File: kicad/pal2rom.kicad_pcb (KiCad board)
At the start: 2 copper layers, 85 x 100 mm, 11 parts, among them J1 PAL2_Expansion, J4 RIOT+, U1 28C256, U2 74LS145

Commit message: Improve addressing
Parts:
- added C2: .1uF, Capacitor_THT:C_Disc_D5.0mm_W2.5mm_P2.50mm, F.Cu at (138.9, 84.6)
- added JP5: A13_INV, Connector_PinHeader_2.54mm:PinHeader_1x03_P2.54mm_Vertical, F.Cu at (123.7, 115.1)
- added JP6: A12_INV, Connector_PinHeader_2.54mm:PinHeader_1x03_P2.54mm_Vertical, F.Cu at (111.0, 115.1)
- added JP7: A11_INV, Connector_PinHeader_2.54mm:PinHeader_1x03_P2.54mm_Vertical, F.Cu at (98.3, 115.1)
- added R1: 1K2, Resistor_THT:R_Axial_DIN0207_L6.3mm_D2.5mm_P7.62mm_Horizontal, F.Cu at (111.0, 49.0)
- added U3: 74LS04, Package_DIP:DIP-14_W7.62mm, F.Cu at (133.9, 89.7)
- U2: footprint Package_DIP:DIP-16_W7.62mm_Socket -> Package_DIP:DIP-16_W7.62mm
- moved C1 13.2 mm to (126.2, 84.6), turned to 180 degrees
- moved JP1 8.03 mm to (95.8, 99.8)
- moved JP4 8.03 mm to (111.0, 99.8)
- moved JP2 7.62 mm to (108.5, 84.6)
- moved JP3 7.62 mm to (98.3, 84.6)
- moved U2 5.08 mm to (121.2, 89.7)
- renumbered C2 to C3
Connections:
- JP1 pad 1: /~{OE} -> /~{CS}
- JP1 pad 3: /~{OE} -> /~{CS}
- JP1 pad 5: /~{OE} -> /~{CS}
- JP2 pad 4: /AB13 -> Net-(JP2-Pin_4)
- JP4 pad 1: /~{OE} -> /~{CS}
- JP4 pad 2: /~{CS} -> /~{OE}
- U1 pad 2: /AB12 -> /A12
- U1 pad 23: /AB11 -> /A11
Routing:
- net Net-(JP7-Pin_3): track 0.00 -> 102.5 mm
- net /A11: track 0.00 -> 85.3 mm
- net /A13: track 126.2 -> 41.3 mm
- net Net-(JP2-Pin_4): track 0.00 -> 69.7 mm
- net /A12: track 0.00 -> 65.9 mm
- net Net-(JP6-Pin_3): track 0.00 -> 60.6 mm
- net VCC: track 109.6 -> 145.7 mm
- net Net-(JP5-Pin_3): track 0.00 -> 34.0 mm
- net /~{OE}: track 112.1 -> 81.6 mm
- net /AB14: track 34.8 -> 63.8 mm
- net /AB11: track 101.9 -> 130.0 mm
- net /AB15: track 31.8 -> 59.6 mm
- net /AB13: track 57.1 -> 76.8 mm
- net /~{CS}: track 101.1 -> 111.4 mm
- net /8K7_ROM: track 45.2 -> 53.7 mm
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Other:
- board text added: "A11"
- board text added: "A12"
- board text added: "A13"
- board text added: "INVERT ADDRESS"
- board text added: "PAL-2 ROM Board Plastic Objects Limited"
- board text added: "ROM BANK"
- board text added: "Rev 0.1 - 10/2026"
- board text added: "~{A11}"
- board text added: "~{A12}"
- board text added: "~{A13}"
- board text removed: "PAL-2 ROM Whatsit Plastic Objects Limited"
- board text removed: "ROM CONFIG"
- board text removed: "Rev 0 - 10/2026"

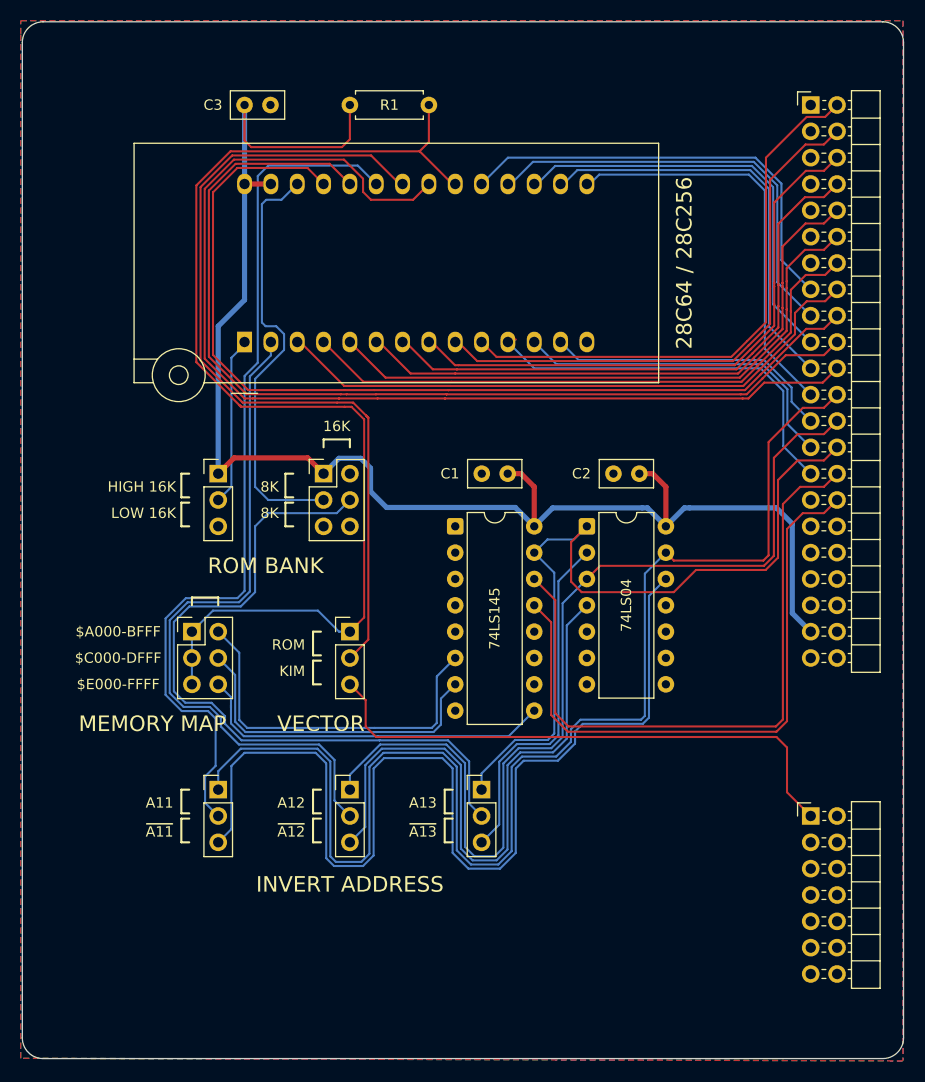
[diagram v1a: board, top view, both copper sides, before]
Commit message: Minor routing improvements
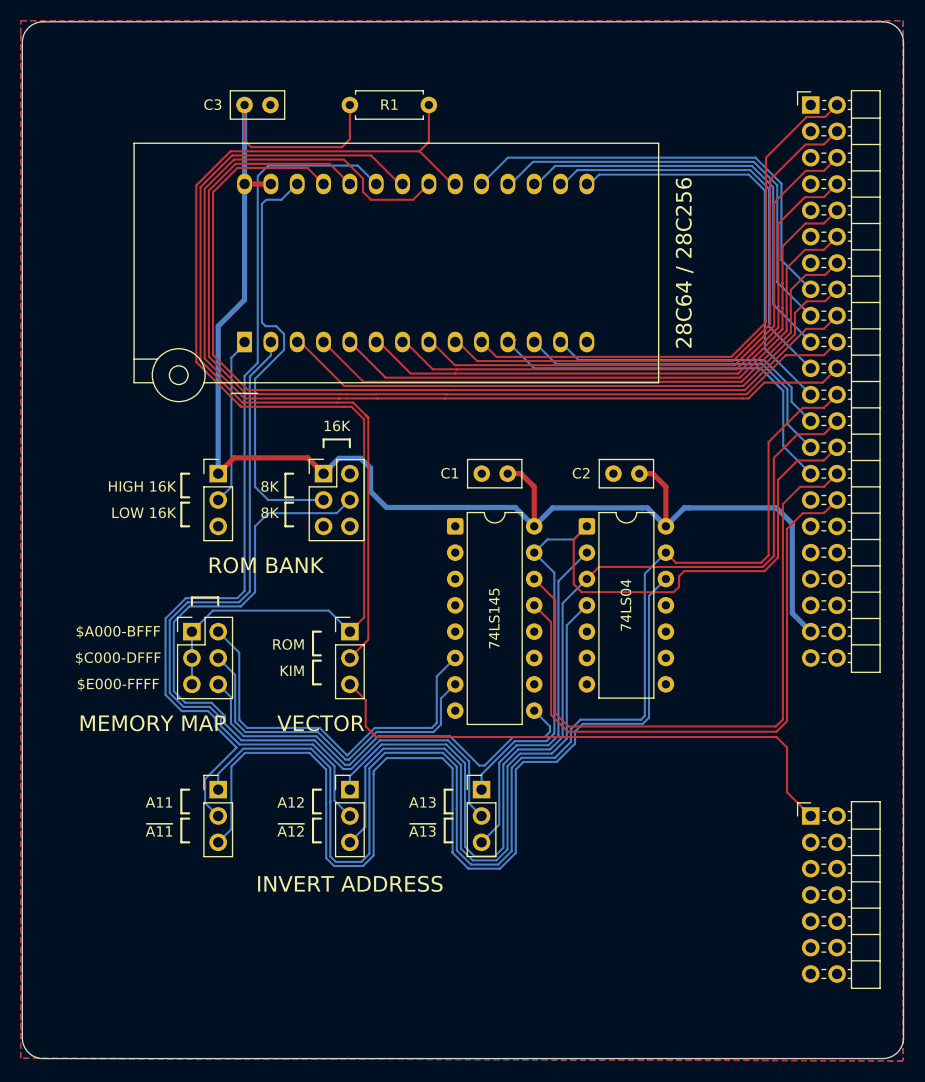
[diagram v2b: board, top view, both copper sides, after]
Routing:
- net /E000-FFFF: track 35.3 -> 43.3 mm
- net Net-(JP2-Pin_4): track 69.7 -> 72.0 mm
- net /A000-BFFF: track 35.9 -> 38.1 mm
- net /C000-DFFF: track 31.8 -> 34.0 mm
- net /A11: track 85.3 -> 87.0 mm
- net Net-(JP7-Pin_3): track 102.5 -> 101.9 mm
